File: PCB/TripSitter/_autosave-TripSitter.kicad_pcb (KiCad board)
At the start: 4 copper layers, 203 x 85 mm, 155 parts, among them IC1 MT25QL256ABA1EW9-0SIT, IC701 IP4220CZ6, J1 Conn_ARM_JTAG_SWD_20, J2 DE15_Plug_HighDensity_Mountin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, J201 Conn_ARM_JTAG_SWD_20, J3 USB_B_Micro, J6 EFM32_PinHeader_PortE, J7 HDMI_A_1.4, J801 Conn_02x05_Odd_Even, J802 Jack-DC, J803 USB_B_Micro, SW1 SW_Push_Open, SW801 SW_DPDT_x2, U1 XC7A100T-FGG484, U2 TPS54325_PWP_14, U201 EFM32GG11B420F2048GQ100, U202 IS62WVS2568FBLL-20NLI, U4 DSC1001DL5-100.0000T, U5 TPS54294PWP, U6 IS62WVS2568FBLL-20NLI, U7 TPD12S520DBT, Y201 48MHz

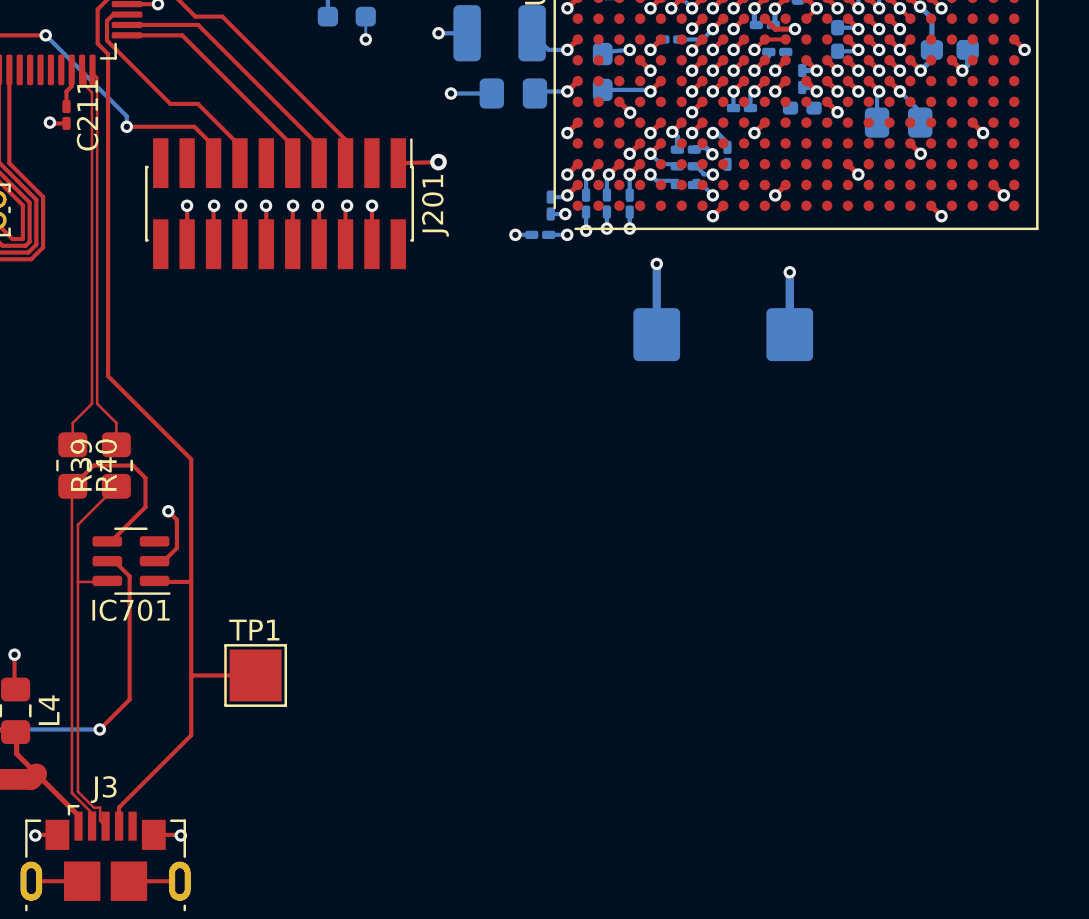
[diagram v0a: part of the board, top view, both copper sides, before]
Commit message: fix power circuit and replace jtag debug
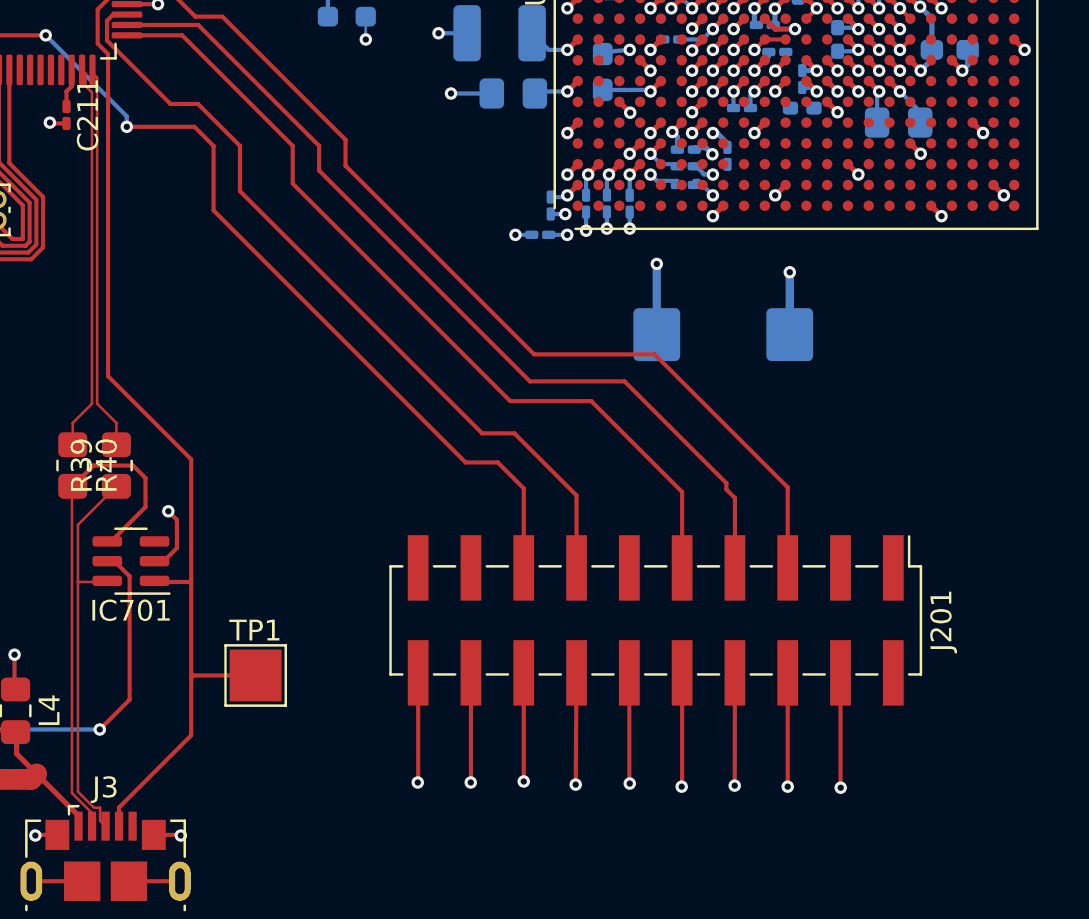
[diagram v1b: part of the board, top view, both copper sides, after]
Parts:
- J201: footprint Connector_PinHeader_1.27mm:PinHeader_2x10_P1.27mm_Vertical_SMD -> Connector_PinHeader_2.54mm:PinHeader_2x10_P2.54mm_Vertical_SMD
- moved J201 27.0 mm to (163.8, 88.5)
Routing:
- net GND: track 578.0 -> 612.0 mm, vias 239 -> 240
- net Net-(J201-TDI): track 14.8 -> 46.4 mm
- net Net-(J201-TMS/SWDIO): track 12.5 -> 42.9 mm
- net Net-(J201-TCK/SWDCLK): track 11.0 -> 40.5 mm
- net Net-(J201-TDO/SWO): track 11.4 -> 38.5 mm
- net EFM32_RESETN: track 73.1 -> 99.7 mm
- net +3.3V: track 100.8 -> 98.9 mm, vias 55 -> 54
